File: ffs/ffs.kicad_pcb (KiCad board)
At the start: 2 copper layers, 34 parts, among them J1 EURO_PWR_2x5, J2 Conn_01x10_Male, U1 4015, U10 4051, U12 4017, U13 4017, U2 4051, U3 4051, U4 4046, U5 4081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

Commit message: ffs routing done
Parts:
- removed the REF** at (45.7, 38.1)
- added C5: 10uf, Capacitor_THT:CP_Radial_D8.0mm_P2.50mm, F.Cu at (85.7, 90.2)
- added C6: 224nf, Capacitor_THT:C_Disc_D4.3mm_W1.9mm_P5.00mm, F.Cu at (115.6, 66.0)
- added C7: 224nf, Capacitor_THT:C_Disc_D4.3mm_W1.9mm_P5.00mm, F.Cu at (115.6, 69.8)
- added REF**: MountingHole_2.2mm_M2, MountingHole:MountingHole_2.2mm_M2, F.Cu at (152.4, 35.6)
- added REF**: MountingHole_2.2mm_M2, MountingHole:MountingHole_2.2mm_M2, F.Cu at (152.4, 103.5)
- added REF**: MountingHole_2.2mm_M2, MountingHole:MountingHole_2.2mm_M2, F.Cu at (45.7, 102.9)
- added REF**: MountingHole_2.2mm_M2, MountingHole:MountingHole_2.2mm_M2, F.Cu at (45.7, 35.6)
- added U11: 40106, Package_DIP:DIP-16_W7.62mm_Socket, F.Cu at (113.7, 40.6)
- C4: value 22uf -> 10uf
- D2, D3, D5, D6: value D -> 1N4148
- TP6: value TestPoint -> -12V
- moved TP5 47.3 mm to (115.6, 94.0), turned to 270 degrees
- moved TP6 43.6 mm to (115.6, 87.0), turned to 270 degrees
- moved TP4 41.5 mm to (115.6, 80.0), turned to 270 degrees
- moved C1 24.1 mm to (83.2, 67.3)
- moved D4 18.1 mm to (148.0, 71.1)
- moved C2 15.8 mm to (73.0, 67.3)
- moved C4 12.1 mm to (85.7, 79.4)
- moved U12 11.4 mm to (127.0, 40.6)
- moved U9 8.25 mm to (140.3, 40.6)
- moved R1 7.10 mm to (111.8, 74.3)
- moved U13 5.72 mm to (121.3, 76.2)
- moved U1 5.08 mm to (66.0, 63.5)
- moved D5 3.42 mm to (148.0, 82.5)
- moved D6 3.18 mm to (148.0, 86.4)
- moved U8 3.18 mm to (142.9, 63.5)
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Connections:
- net D2A renamed D2
- J2 pad 5: MR1 -> D1
- J2 pad 6: D1A -> CP2
- J2 pad 7: D1B -> MR
- J2 pad 9: D2B -> GND
- U1 pad 14: MR1 -> MR
- U1 pad 15: D1B -> Net-(U1-Pad10)
- U1 pad 16: Vdd -> +12V
- U1 pad 6: MR1 -> MR
- U1 pad 7: D1A -> D1
- U1 pad 8: Vss -> GND
- U12 pad 3: FreqDivOut -> Net-(U12-Pad3)
- U13 pad 1: Net-(U10-Pad5) -> Net-(U10-Pad1)
- U13 pad 10: Net-(U10-Pad1) -> Net-(U10-Pad12)
- U13 pad 11: Net-(U13-Pad11) -> Net-(D6-Pad2)
- U13 pad 15: FreqDivOut -> Net-(U12-Pad3)
- U13 pad 2: Net-(U10-Pad14) -> Net-(U10-Pad13)
- U13 pad 3: Net-(U10-Pad13) -> Net-(U13-Pad3)
- U13 pad 4: Net-(U10-Pad15) -> Net-(U10-Pad14)
- U13 pad 5: Net-(U10-Pad2) -> Net-(U10-Pad5)
- U13 pad 6: Net-(U10-Pad4) -> Net-(U10-Pad2)
- U13 pad 7: Net-(U10-Pad12) -> Net-(U10-Pad15)
- U13 pad 9: Net-(D6-Pad2) -> Net-(U10-Pad4)
- U4 pad 14: SigIn -> Net-(U11-Pad2)
- U4 pad 4: FreqMulOut -> FreqMultOut
- U5 pad 1: Net-(U2-Pad4) -> Net-(U5-Pad1)
- U5 pad 10: (no net) -> Net-(U13-Pad14)
- U5 pad 11: (no net) -> Net-(C7-Pad2)
- U5 pad 12: (no net) -> FreqMultOut
- U5 pad 13: (no net) -> Net-(U12-Pad3)
- U5 pad 4: Net-(U13-Pad14) -> Net-(C6-Pad1)
- U5 pad 5: Net-(U12-Pad11) -> FreqMultOut
- U5 pad 6: FreqMultOut -> Net-(U5-Pad6)
- U5 pad 8: (no net) -> Net-(U12-Pad11)
- U5 pad 9: (no net) -> FreqMultOut
- U6 pad 1: Net-(U2-Pad12) -> Net-(U2-Pad1)
- U6 pad 10: Net-(U2-Pad15) -> Net-(U2-Pad12)
- U6 pad 11: Net-(U2-Pad4) -> Net-(U5-Pad1)
- U6 pad 13: Net-(U2-Pad4) -> Net-(U5-Pad1)
- U6 pad 2: Net-(U6-Pad2) -> Net-(U2-Pad13)
- U6 pad 3: SigIn -> Net-(U5-Pad6)
- U6 pad 4: Net-(U2-Pad13) -> Net-(U2-Pad14)
- U6 pad 5: Net-(U2-Pad1) -> Net-(U2-Pad5)
- U6 pad 6: Net-(U2-Pad5) -> Net-(U2-Pad2)
- U6 pad 7: Net-(U2-Pad14) -> Net-(U2-Pad15)
- U6 pad 9: Net-(U2-Pad2) -> Net-(U2-Pad4)
- U7 pad 1: Net-(U3-Pad5) -> Net-(U3-Pad1)
- U7 pad 10: Net-(U3-Pad1) -> Net-(U3-Pad12)
- U7 pad 11: Net-(U7-Pad11) -> Net-(D3-Pad2)
- U7 pad 15: SigIn -> Net-(U5-Pad6)
- U7 pad 2: Net-(U3-Pad14) -> Net-(U3-Pad13)
- U7 pad 3: Net-(U3-Pad13) -> Net-(U7-Pad3)
- U7 pad 4: Net-(U3-Pad15) -> Net-(U3-Pad14)
- U7 pad 5: Net-(U3-Pad2) -> Net-(U3-Pad5)
- U7 pad 6: Net-(U3-Pad4) -> Net-(U3-Pad2)
- U7 pad 7: Net-(U3-Pad12) -> Net-(U3-Pad15)
- U7 pad 9: Net-(D3-Pad2) -> Net-(U3-Pad4)
- U8 pad 1: CP1 -> CP2
- U8 pad 14: MR1 -> MR
- U8 pad 15: D2B -> Net-(U8-Pad10)
- U8 pad 16: Vdd -> +12V
- U8 pad 6: MR1 -> MR
- U8 pad 8: Vss -> GND
- U8 pad 9: CP1 -> CP2
- U9 pad 1: Net-(U12-Pad5) -> Net-(U12-Pad1)
- U9 pad 12: Net-(U12-Pad1) -> Net-(U12-Pad10)
- U9 pad 13: Net-(U12-Pad4) -> Net-(U12-Pad2)
- U9 pad 14: Net-(U12-Pad7) -> Net-(U12-Pad4)
- U9 pad 15: Net-(U12-Pad10) -> Net-(U12-Pad7)
- U9 pad 2: Net-(U12-Pad9) -> Net-(U12-Pad6)
- U9 pad 4: Net-(U12-Pad11) -> Net-(U12-Pad9)
- U9 pad 5: Net-(U12-Pad6) -> Net-(U12-Pad5)
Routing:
- net +12V: track 99.3 -> 257.2 mm, vias 0 -> 2
- net MR: track 0.00 -> 133.9 mm, vias 0 -> 1
- net FreqMultOut: track 17.8 -> 143.8 mm, vias 0 -> 2
- net GND: track 2.54 -> 102.7 mm
- net CP2: track 0.00 -> 79.4 mm
- net -12V: track 0.00 -> 72.9 mm, vias 0 -> 1
- net Net-(U5-Pad6): track 0.00 -> 68.1 mm, vias 0 -> 1
- net Net-(U12-Pad3): track 0.00 -> 68.0 mm, vias 0 -> 1
- net D1: track 0.00 -> 64.9 mm
- net Net-(U12-Pad11): track 0.00 -> 61.9 mm
- net D1A: track 57.4 -> 0.00 mm, vias 1 -> 0
- net D2: track 0.00 -> 56.5 mm
- net Net-(C7-Pad2): track 0.00 -> 50.9 mm, vias 0 -> 1
- net Net-(D4-Pad1): track 0.00 -> 50.9 mm
- net Net-(U11-Pad2): track 0.00 -> 50.3 mm
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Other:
- net class GND added: clearance 0.2, trace_width 0.25, via_dia 0.8, via_drill 0.4
- board text added: "WibWob V4000 Fractional Frequency Synthesizer"

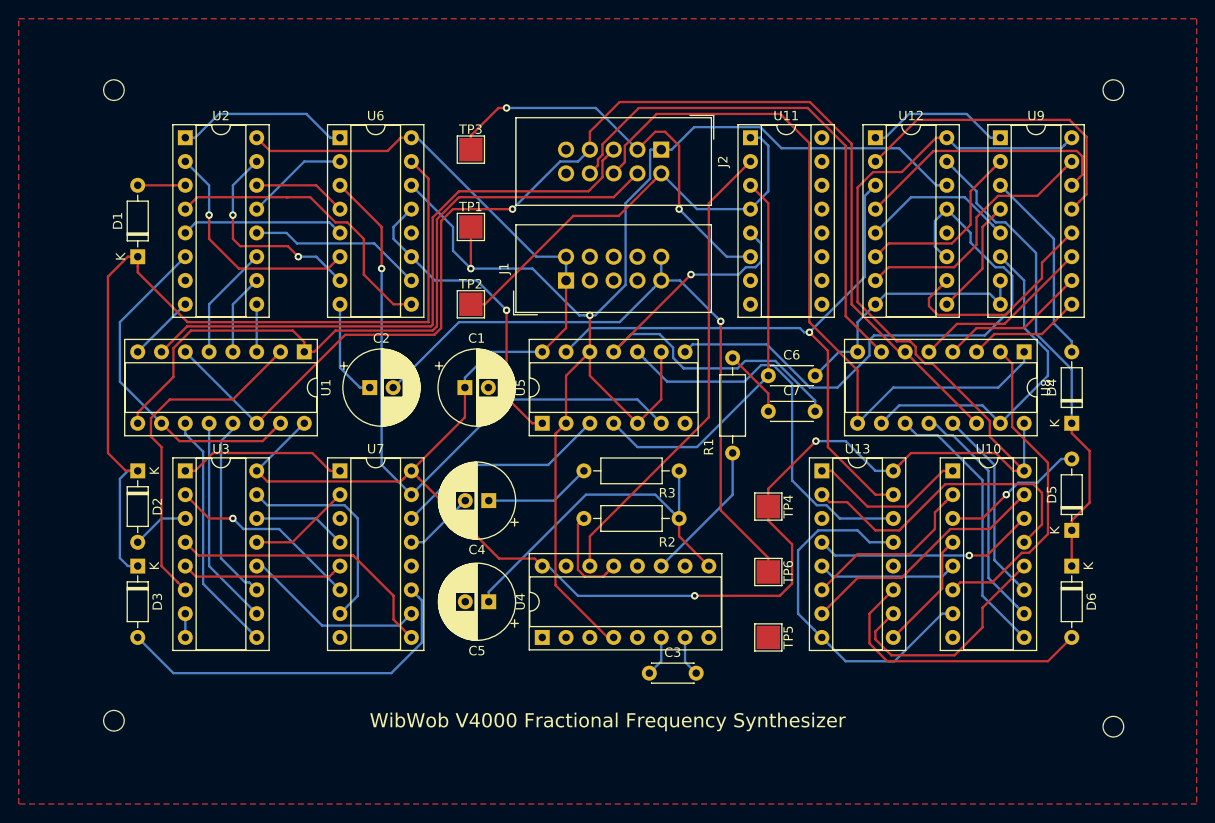
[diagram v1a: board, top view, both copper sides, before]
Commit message: added bypass caps
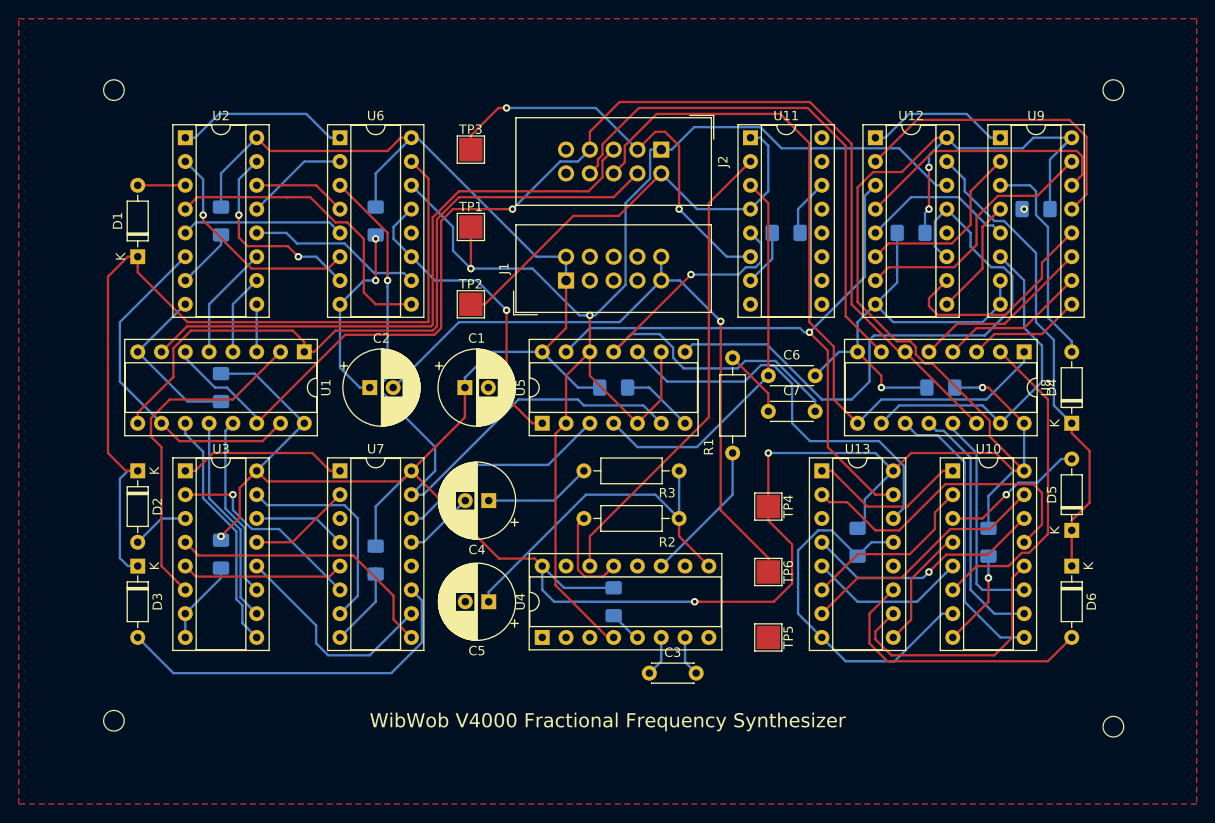
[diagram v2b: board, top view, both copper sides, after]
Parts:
- added C10: 10nf, Capacitor_SMD:C_1206_3216Metric_Pad1.42x1.75mm_HandSolder, B.Cu at (57.1, 67.3)
- added C11: 10nf, Capacitor_SMD:C_1206_3216Metric_Pad1.42x1.75mm_HandSolder, B.Cu at (57.1, 49.5)
- added C12: 10nf, Capacitor_SMD:C_1206_3216Metric_Pad1.42x1.75mm_HandSolder, B.Cu at (144.1, 48.3)
- added C13: 10nf, Capacitor_SMD:C_1206_3216Metric_Pad1.42x1.75mm_HandSolder, B.Cu at (73.7, 49.5)
- added C14: 10nf, Capacitor_SMD:C_1206_3216Metric_Pad1.42x1.75mm_HandSolder, B.Cu at (130.8, 50.8)
- added C15: 10nf, Capacitor_SMD:C_1206_3216Metric_Pad1.42x1.75mm_HandSolder, B.Cu at (139.1, 83.8)
- added C16: 10nf, Capacitor_SMD:C_1206_3216Metric_Pad1.42x1.75mm_HandSolder, B.Cu at (134.0, 67.3)
- added C18: 10nf, Capacitor_SMD:C_1206_3216Metric_Pad1.42x1.75mm_HandSolder, B.Cu at (99.1, 90.2)
- added C19: 10nf, Capacitor_SMD:C_1206_3216Metric_Pad1.42x1.75mm_HandSolder, B.Cu at (117.5, 50.8)
- added C20: 10nf, Capacitor_SMD:C_1206_3216Metric_Pad1.42x1.75mm_HandSolder, B.Cu at (99.1, 67.3)
- added C21: 10nf, Capacitor_SMD:C_1206_3216Metric_Pad1.42x1.75mm_HandSolder, B.Cu at (125.1, 83.8)
- added C8: 10nf, Capacitor_SMD:C_1206_3216Metric_Pad1.42x1.75mm_HandSolder, B.Cu at (73.7, 85.7)
- added C9: 10nf, Capacitor_SMD:C_1206_3216Metric_Pad1.42x1.75mm_HandSolder, B.Cu at (57.1, 85.1)
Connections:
- U11 pad 14: Net-(U11-Pad14) -> +12V
- U11 pad 7: Net-(U11-Pad7) -> GND
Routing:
- net +12V: track 257.2 -> 376.4 mm, vias 2 -> 6
- net GND: track 102.7 -> 193.1 mm, vias 0 -> 5
- net Net-(U3-Pad12): track 19.7 -> 24.0 mm
- net Net-(U12-Pad11): track 61.9 -> 64.8 mm
- net Net-(U10-Pad11): track 20.9 -> 23.5 mm
- net Net-(U5-Pad6): track 68.1 -> 70.7 mm
- net Net-(U10-Pad12): track 25.3 -> 27.8 mm
- net Net-(U10-Pad5): track 14.9 -> 17.1 mm
- net Net-(U10-Pad14): track 23.8 -> 25.8 mm
- net Net-(D4-Pad2): track 20.9 -> 22.8 mm
- net Net-(U10-Pad10): track 25.3 -> 26.8 mm
- net Net-(U10-Pad9): track 29.4 -> 30.9 mm
- net Net-(U13-Pad14): track 42.2 -> 43.5 mm
- net Net-(U2-Pad4): track 31.9 -> 33.0 mm
- net Net-(U2-Pad15): track 22.6 -> 21.6 mm
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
